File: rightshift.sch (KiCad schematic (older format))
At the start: 15 parts

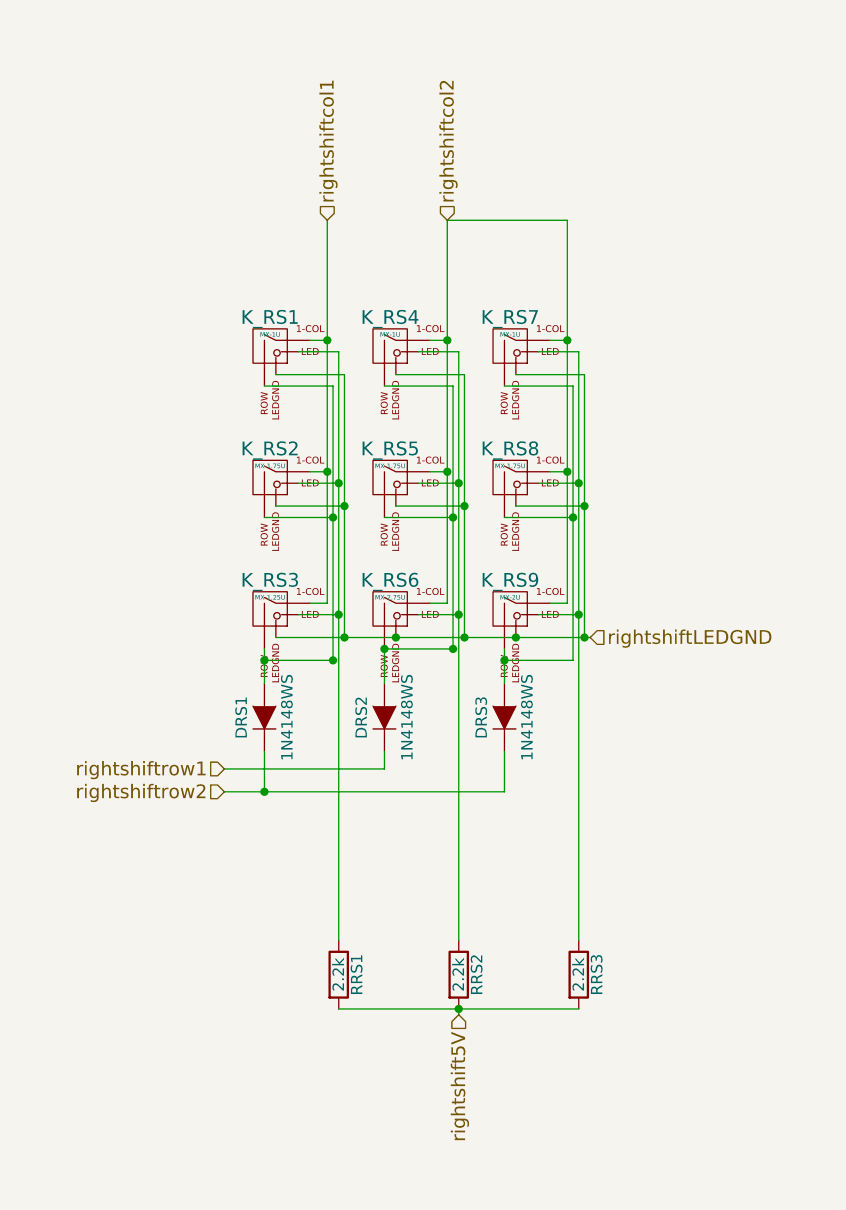
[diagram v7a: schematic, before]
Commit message: Flipped schematic symbols for keys (except LS and bottom right mods)
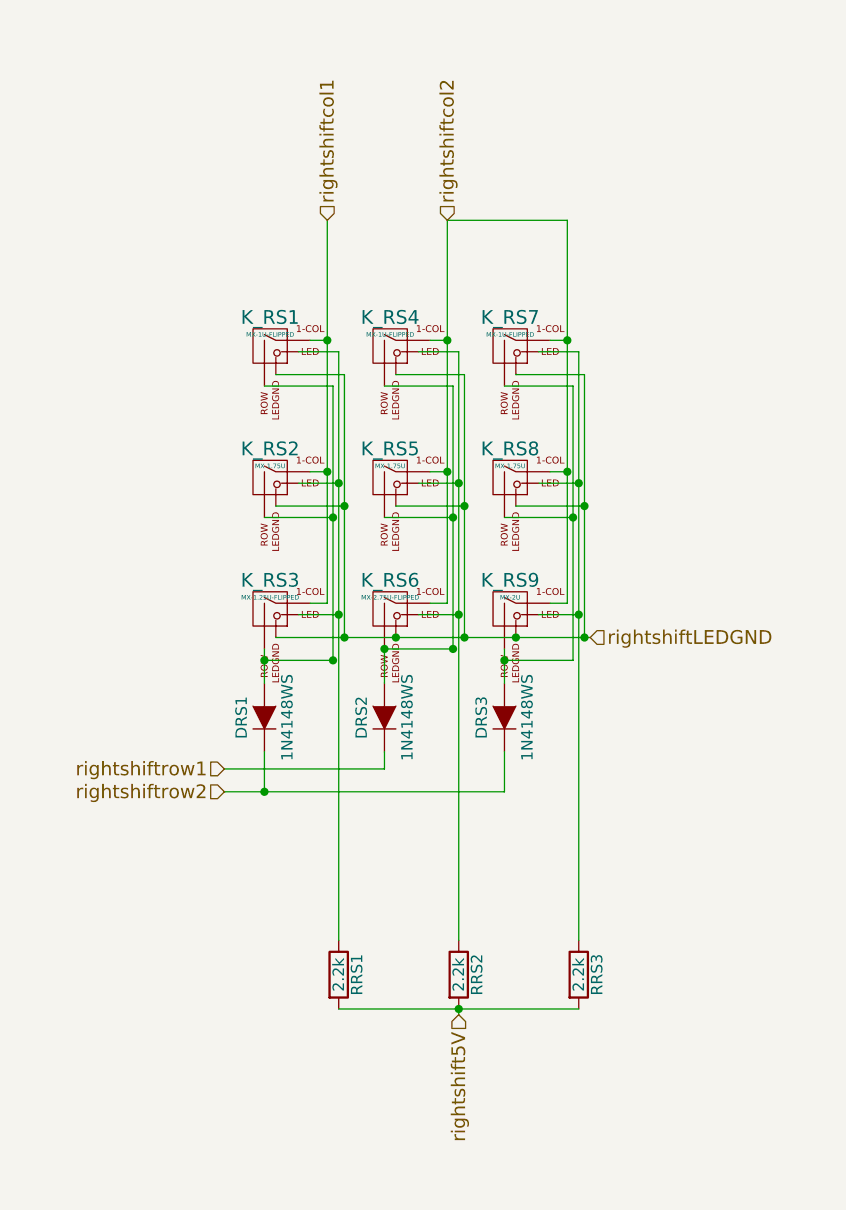
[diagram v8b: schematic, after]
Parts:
- removed K_RS1, K_RS4, K_RS7: MX-1U, MX_Alps_Hybrid:MX-1U, symbol MX-1U
- removed K_RS3: MX-1.25U, MX_Alps_Hybrid:MX-1.25U, symbol MX-1.25U
- removed K_RS6: MX-2.75U, MX_Alps_Hybrid:MX-2.75U, symbol MX-2.75U
- added K_RS1, K_RS4, K_RS7: MX-1U-FLIPPED, symbol MX-1U-FLIPPED
- added K_RS3: MX-1.25U-FLIPPED, symbol MX-1.25U-FLIPPED
- added K_RS6: MX-2.75U-FLIPPED, symbol MX-2.75U-FLIPPED
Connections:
- net rightshiftLEDGND: now also K_RS1.4 (LEDGND), K_RS3.4 (LEDGND), K_RS4.4 (LEDGND), K_RS6.4 (LEDGND), K_RS7.4 (LEDGND)
- net rightshiftcol1: now also K_RS1.2 (COL), K_RS3.2 (COL)
- net rightshiftcol2: now also K_RS4.2 (COL), K_RS6.2 (COL), K_RS7.2 (COL)
- net at DRS1.2 (A), K_RS2.2 (ROW): now also K_RS1.1 (ROW), K_RS3.1 (ROW)
- net at K_RS2.3 (LED), RRS1.1: now also K_RS1.3 (LED), K_RS3.3 (LED)
- net at DRS2.2 (A), K_RS5.2 (ROW): now also K_RS4.1 (ROW), K_RS6.1 (ROW)
- net at K_RS5.3 (LED), RRS2.1: now also K_RS4.3 (LED), K_RS6.3 (LED)
- net at DRS3.2 (A), K_RS8.2 (ROW), K_RS9.2 (ROW): now also K_RS7.1 (ROW)
- net at K_RS8.3 (LED), K_RS9.3 (LED), RRS3.1: now also K_RS7.3 (LED)
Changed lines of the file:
@@
 $EndDescr
-$Comp
-L MX-1U K_RS1
-U 1 1 591D166F
-P 4800 2250
-F 0 "K_RS1" H 4800 2375 60  0000 C CNN
-F 1 "MX-1U" H 4800 2300 20  0000 C CNN
-F 2 "MX_Alps_Hybrid:MX-1U" H 4775 2225 60  0001 C CNN
-F 3 "" H 4775 2225 60  0001 C CNN
-	1    4800 2250
-	1    0    0    -1
-$EndComp
-$Comp
-L MX-1.25U K_RS2
-U 1 1 591D16FE
-P 4800 2825
-F 0 "K_RS2" H 4800 2950 60  0000 C CNN
-F 1 "MX-1.75U" H 4800 2875 20  0000 C CNN
-F 2 "MX_Alps_Hybrid:MX-1.75U" H 4775 2800 60  0001 C CNN
-F 3 "" H 4775 2800 60  0001 C CNN
-	1    4800 2825
-	1    0    0    -1
-$EndComp
-$Comp
-L MX-1.25U K_RS3
-U 1 1 591D173D
-P 4800 3400
-F 0 "K_RS3" H 4800 3525 60  0000 C CNN
-F 1 "MX-1.25U" H 4800 3450 20  0000 C CNN
-F 2 "MX_Alps_Hybrid:MX-1.25U" H 4775 3375 60  0001 C CNN
-F 3 "" H 4775 3375 60  0001 C CNN
-	1    4800 3400
-	1    0    0    -1
-$EndComp
-$Comp
-L MX-1U K_RS4
-U 1 1 591D189D
-P 5325 2250
-F 0 "K_RS4" H 5325 2375 60  0000 C CNN
-F 1 "MX-1U" H 5325 2300 20  0000 C CNN
-F 2 "MX_Alps_Hybrid:MX-1U" H 5300 2225 60  0001 C CNN
-F 3 "" H 5300 2225 60  0001 C CNN
-	1    5325 2250
-	1    0    0    -1
-$EndComp
 $Comp
 L MX-1.75U K_RS5
@@
 F 3 "" H 5300 2800 60  0001 C CNN
 	1    5325 2825
-	1    0    0    -1
-$EndComp
-$Comp
-L MX-2.75U K_RS6
-U 1 1 591D1A90
-P 5325 3400
-F 0 "K_RS6" H 5325 3525 60  0000 C CNN
-F 1 "MX-2.75U" H 5325 3450 20  0000 C CNN
-F 2 "MX_Alps_Hybrid:MX-2.75U" H 5300 3375 60  0001 C CNN
-F 3 "" H 5300 3375 60  0001 C CNN
-	1    5325 3400
-	1    0    0    -1
-$EndComp
-$Comp
-L MX-1U K_RS7
-U 1 1 591D21A1
-P 5850 2250
-F 0 "K_RS7" H 5850 2375 60  0000 C CNN
-F 1 "MX-1U" H 5850 2300 20  0000 C CNN
-F 2 "MX_Alps_Hybrid:MX-1U" H 5825 2225 60  0001 C CNN
-F 3 "" H 5825 2225 60  0001 C CNN
-	1    5850 2250
 	1    0    0    -1
 $EndComp
@@
 	5825 4200 5825 4025
 Connection ~ 4775 4200
+$Comp
+L MX-1U-FLIPPED K_RS7
+U 1 1 598DC160
+P 5850 2250
+F 0 "K_RS7" H 5850 2375 60  0000 C CNN
+F 1 "MX-1U-FLIPPED" H 5850 2300 20  0000 C CNN
+F 2 "" H 5825 2225 60  0001 C CNN
+F 3 "" H 5825 2225 60  0001 C CNN
+	1    5850 2250
+	1    0    0    -1
+$EndComp
+$Comp
+L MX-1U-FLIPPED K_RS4
+U 1 1 598DC28B
+P 5325 2250
+F 0 "K_RS4" H 5325 2375 60  0000 C CNN
+F 1 "MX-1U-FLIPPED" H 5325 2300 20  0000 C CNN
+F 2 "" H 5300 2225 60  0001 C CNN
+F 3 "" H 5300 2225 60  0001 C CNN
+	1    5325 2250
+	1    0    0    -1
+$EndComp
+$Comp
+L MX-2.75U-FLIPPED K_RS6
+U 1 1 598DC67F
+P 5325 3400
+F 0 "K_RS6" H 5325 3525 60  0000 C CNN
+F 1 "MX-2.75U-FLIPPED" H 5325 3450 20  0000 C CNN
+F 2 "" H 5300 3375 60  0001 C CNN
+F 3 "" H 5300 3375 60  0001 C CNN
+	1    5325 3400
+	1    0    0    -1
+$EndComp
+$Comp
+L MX-1.25U K_RS2
+U 1 1 591D16FE
+P 4800 2825
+F 0 "K_RS2" H 4800 2950 60  0000 C CNN
+F 1 "MX-1.75U" H 4800 2875 20  0000 C CNN
+F 2 "MX_Alps_Hybrid:MX-1.75U" H 4775 2800 60  0001 C CNN
+F 3 "" H 4775 2800 60  0001 C CNN
+	1    4800 2825
+	1    0    0    -1
+$EndComp
+$Comp
+L MX-1U-FLIPPED K_RS1
+U 1 1 598DC8DE
+P 4800 2250
+F 0 "K_RS1" H 4800 2375 60  0000 C CNN
+F 1 "MX-1U-FLIPPED" H 4800 2300 20  0000 C CNN
+F 2 "" H 4775 2225 60  0001 C CNN
+F 3 "" H 4775 2225 60  0001 C CNN
+	1    4800 2250
+	1    0    0    -1
+$EndComp
+$Comp
+L MX-1.25U-FLIPPED K_RS3
+U 1 1 598DC94B
+P 4800 3400
+F 0 "K_RS3" H 4800 3525 60  0000 C CNN
+F 1 "MX-1.25U-FLIPPED" H 4800 3450 20  0000 C CNN
+F 2 "" H 4775 3375 60  0001 C CNN
+F 3 "" H 4775 3375 60  0001 C CNN
+	1    4800 3400
+	1    0    0    -1
+$EndComp
 $EndSCHEMATC
